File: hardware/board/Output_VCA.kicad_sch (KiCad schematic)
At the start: 23 parts

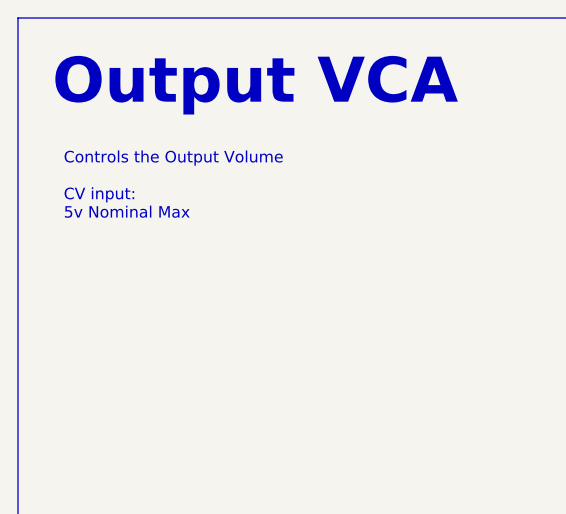
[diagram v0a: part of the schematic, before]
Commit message: Schematic getting closer to being finished
Schematic should be close to being ready to assign MPNs.
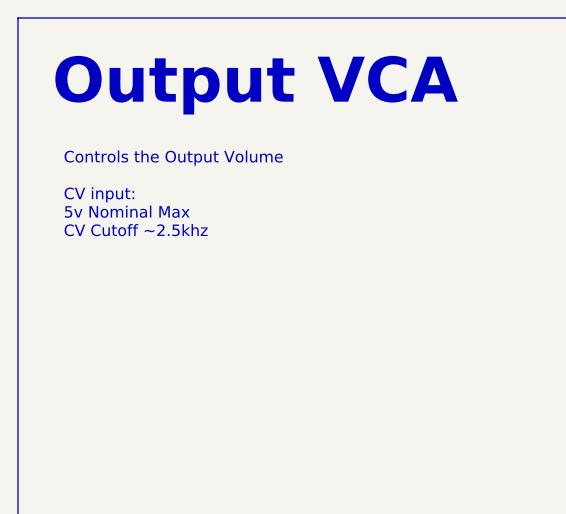
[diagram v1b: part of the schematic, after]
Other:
- note added: "Controls the Output Volume CV input: 5v Nominal Max CV Cutoff ~2.5khz"
- note removed: "Controls the Output Volume CV input: 5v Nominal Max"
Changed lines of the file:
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@@
     (fill (type none))
   )
-  (text "Controls the Output Volume\n\nCV input:\n5v Nominal Max\n\n\n"
+  (text "Controls the Output Volume\n\nCV input:\n5v Nominal Max\nCV Cutoff ~2.5khz\n\n"
     (at 27.94 49.53 0)
     (effects (font (size 1.27 1.27)) (justify left bottom))

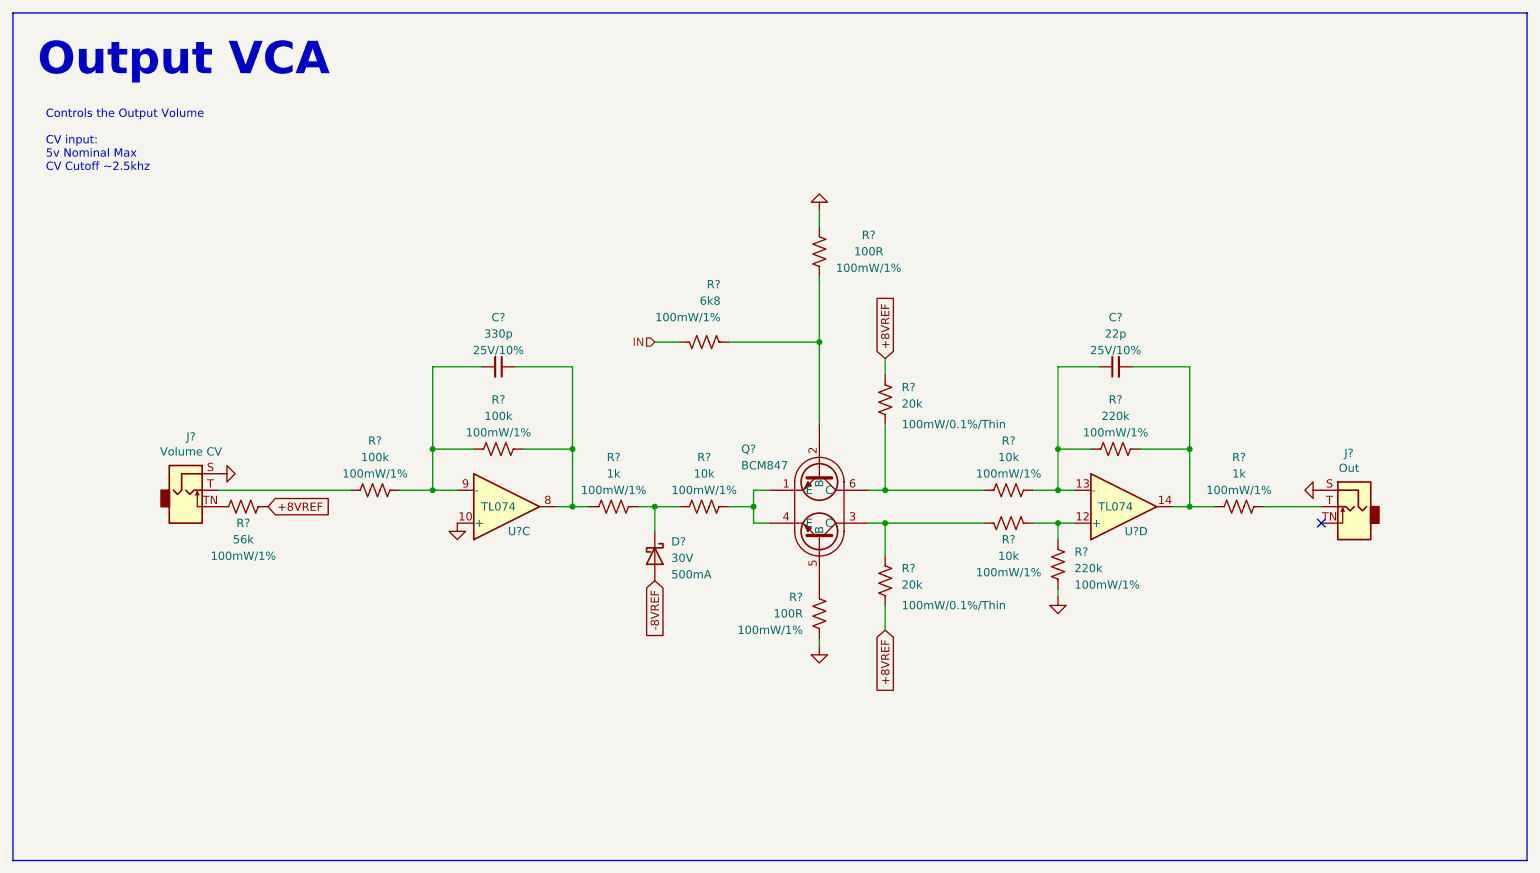
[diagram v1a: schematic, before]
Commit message: BOM Consolidation
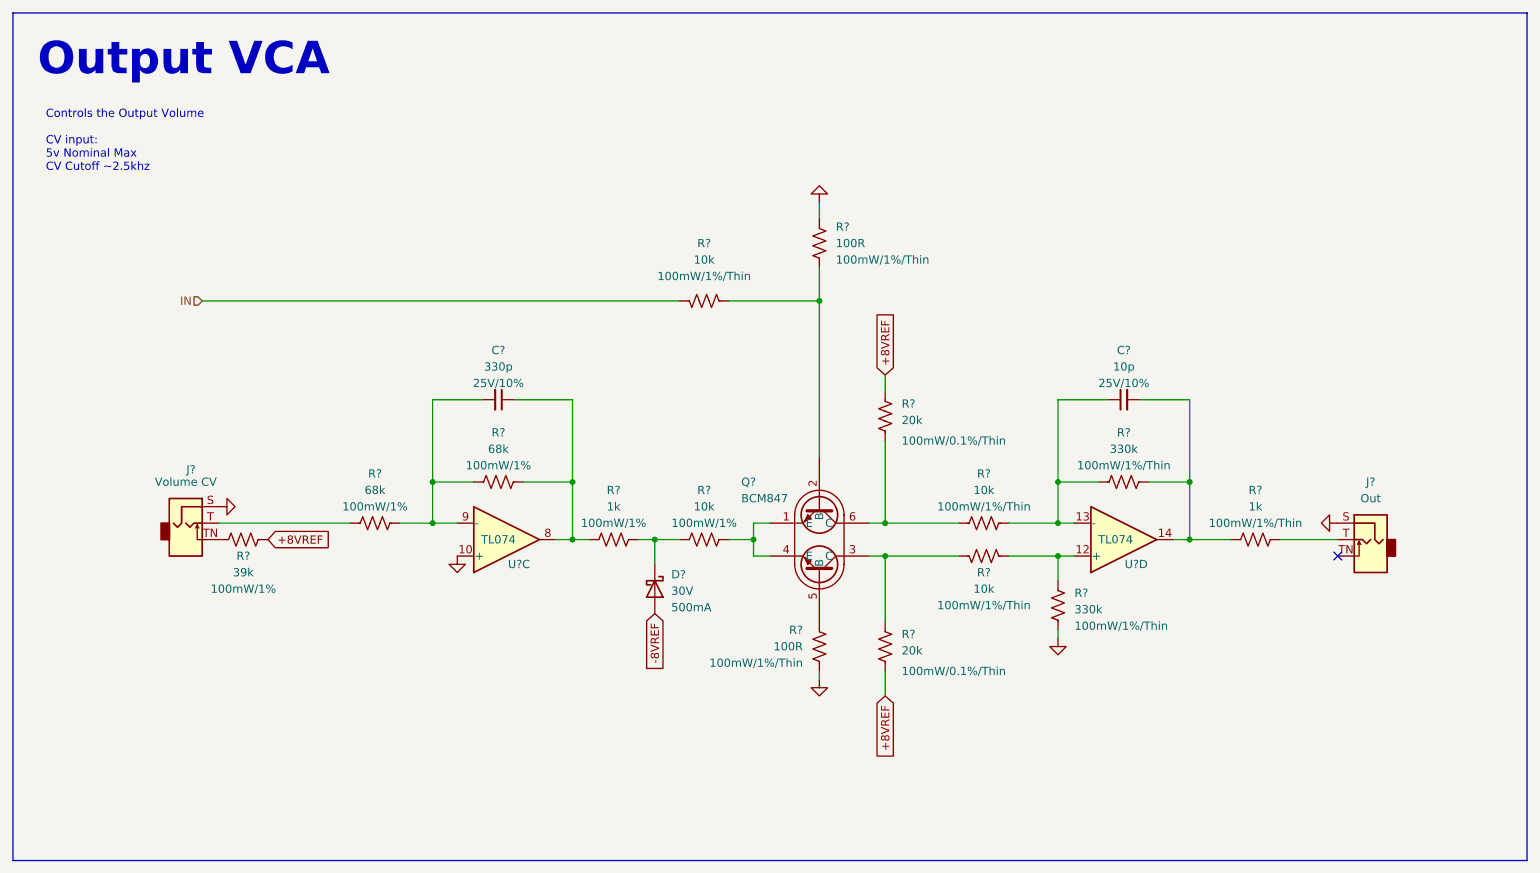
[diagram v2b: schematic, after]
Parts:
- C?: value 22p -> 10p
- J?: value Out -> ~; Name (none) -> Out
- J?: value Volume CV -> ~; Name (none) -> Volume CV
- R? (x2): value 100k -> 68k
- R?: value 6k8 -> 10k; Rating 100mW/1% -> 100mW/1%/Thin
- R? (x5): Rating 100mW/1% -> 100mW/1%/Thin
- R? (x2): value 220k -> 330k; Rating 100mW/1% -> 100mW/1%/Thin
- R?: value 56k -> 39k
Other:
- moved on the sheet: C?, D?, J?, Q?, R?, U?C, U?D

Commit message: Updates for LED Drivers
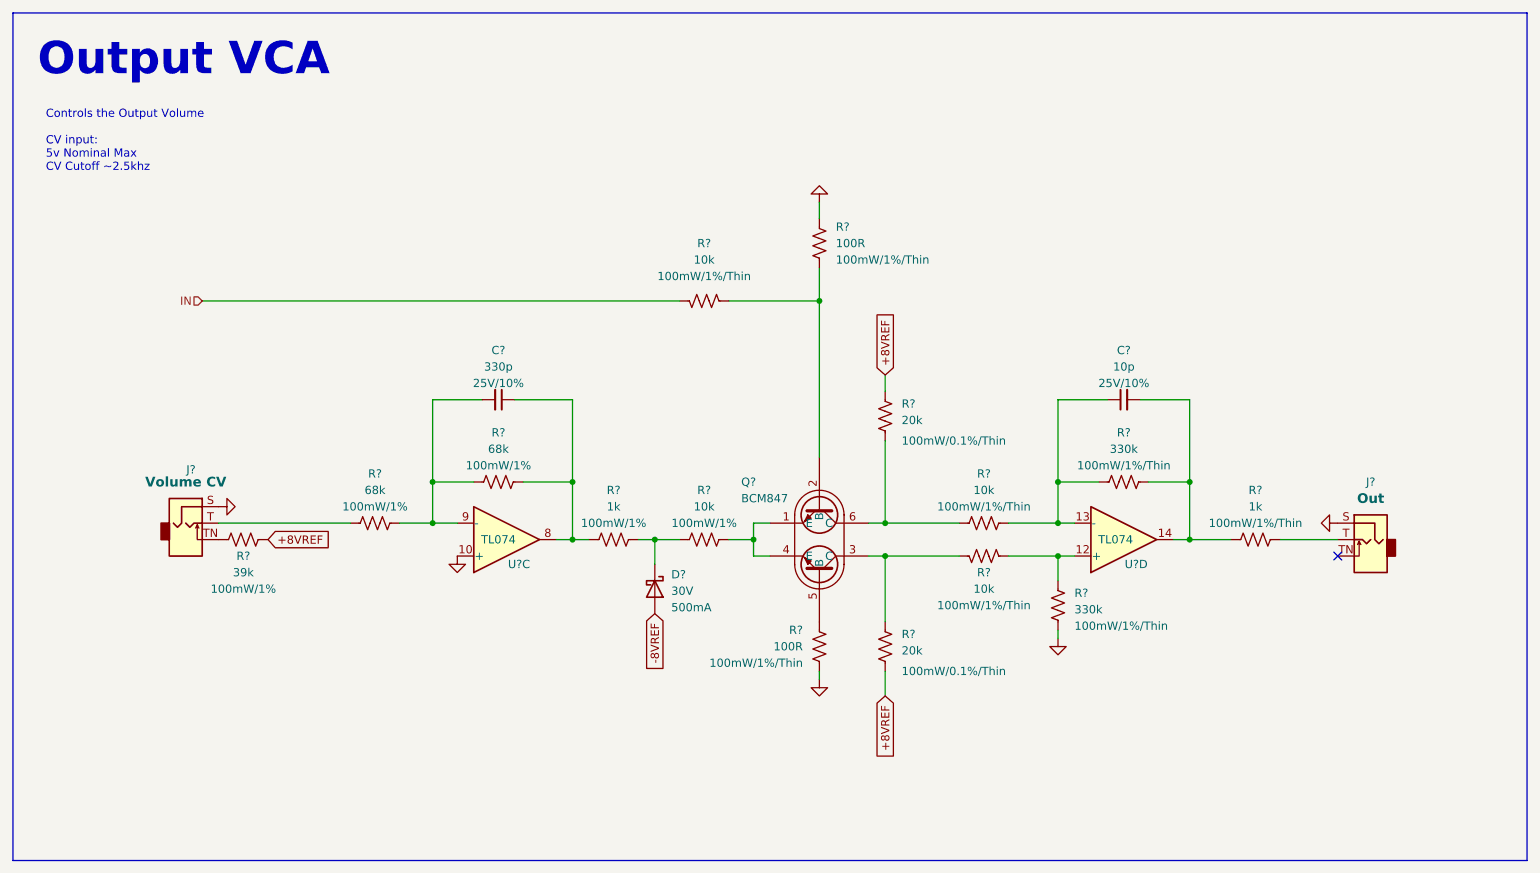
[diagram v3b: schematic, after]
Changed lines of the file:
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@@
     )
     (property "Name" "Out" (at 232.41 97.79 0)
-      (effects (font (size 1.27 1.27)))
+      (effects (font (size 1.5 1.5) bold))
     )
     (pin "S")
@@
     )
     (property "Name" "Volume CV" (at 49.53 95.25 0)
-      (effects (font (size 1.27 1.27)))
+      (effects (font (size 1.5 1.5) bold))
     )
     (pin "S")

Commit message: hardware: update schematic with footprints and preliminary MPNs
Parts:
- C? (x2): Notes 0603, 25V+, 10% -> (none); smd kit 1 -> (none)
- D?: value 30V -> BAS315; footprint winterbloom:D_SOD-123+SOD-123F -> winterbloom:D_SOD-323; MPN (none) -> BAS316,115; Notes Any PMEGxxxxEGW part, 500mA If -> Clipping diode; Rating 500mA -> 1Vf @ 100mA; mpn PMEG2005EGWX -> (none); smd kit 1 -> (none)
- J? (x2): mpn WQP-WQP518MA -> (none)
- Q?: LCSC C396099 -> (none); LCSC Extended YES -> (none); Manufacturer Nexperia -> (none)
- R? (x15): smd kit 1 -> (none)
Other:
- title: Diode Ladder Filter -> Neptune

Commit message: Very first component layout.
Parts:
- removed U?: TL074, Package_SO:TSSOP-14_4.4x5mm_P0.65mm, symbol winterbloom:TL074
- added U?: TL074, Package_SO:TSSOP-14_4.4x5mm_P0.65mm, symbol winterbloom:TL074
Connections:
- net GND: now also U?.12 (+)
- net at C?.2, R?.1, R?.2: now also U?.13 (-)
- net at R?.1, R?.1: now also U?.3 (+); no longer U?.12 (+)
- net at C?.2, R?.1, R?.2: now also U?.1; no longer U?.14
- net at C?.1, R?.1, R?.2: now also U?.2 (-); no longer U?.13 (-)
- net at C?.1, R?.1, R?.2: now also U?.14
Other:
- moved on the sheet: U?D

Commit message: First Draft of layout V2 (All components facing the same way)
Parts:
- removed U? (x2): TL074, Package_SO:TSSOP-14_4.4x5mm_P0.65mm, symbol winterbloom:TL074
- added U? (x2): TL074, Package_SO:TSSOP-14_4.4x5mm_P0.65mm, symbol winterbloom:TL074
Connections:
- net GND: now also U?.10 (+)
- net at C?.2, R?.1, R?.2: now also U?.9 (-)
- net at R?.1, R?.1: now also U?.5 (+)
- net at C?.2, R?.1, R?.2: now also U?.7
- net at C?.1, R?.1, R?.2: now also U?.6 (-)
- net at C?.1, R?.1, R?.2: now also U?.8

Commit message: Rough Draft of Routing Complete. Ugly but Passes DRC
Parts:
- removed D?: BAS315, winterbloom:D_SOD-323, symbol Diode:1N5819
- added D?: BAS315, winterbloom:D_SOD-323, symbol Device:D_Small
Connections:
- net -8VREF: now also D?.2 (A)
- net at R?.1, R?.2: now also D?.1 (K)
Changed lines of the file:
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@@
+    (stroke (width 0) (type default))
+  )
+  (wire (pts (xy 121.92 113.03) (xy 121.92 115.57))
     (stroke (width 0) (type default))
   )
@@
     )
   )
+  (symbol (lib_id "Device:D_Small") (at 121.92 110.49 90) (mirror x) (unit 1)
+    (in_bom yes) (on_board yes) (dnp no)
+    (property "Reference" "D?" (at 131.445 107.95 90)
+      (effects (font (size 1.27 1.27)))
+    )
+    (property "Value" "BAS315" (at 131.445 110.49 90)
+      (effects (font (size 1.27 1.27)))
+    )
+    (property "Footprint" "winterbloom:D_SOD-323" (at 121.92 110.49 90)
+      (effects (font (size 1.27 1.27)) hide)
+    )
+    (property "Datasheet" "~" (at 121.92 110.49 90)
+      (effects (font (size 1.27 1.27)) hide)
+    )
+    (property "MPN" "BAS316,115" (at 121.92 110.49 0)
+      (effects (font (size 1.27 1.27)) hide)
+    )
+    (property "Rating" "1Vf @ 100mA" (at 131.445 113.03 90)
+      (effects (font (size 1.27 1.27)))
+    )
+    (property "Notes" "Clipping diode" (at 121.92 110.49 0)
+      (effects (font (size 1.27 1.27)) hide)
+    )
+    (pin "1")
+    (pin "2")
+    (instances
+      (project "mainboard"
+        (path "/960bd036-bf0c-45ea-9f41-1321756e0e5a"
+          (reference "D?") (unit 1)
+        )
+        (path "/960bd036-bf0c-45ea-9f41-1321756e0e5a/3b1fa3f2-493c-449c-a2d6-10ea677680a0"
+          (reference "D?") (unit 1)
+        )
+        (path "/960bd036-bf0c-45ea-9f41-1321756e0e5a/48d891c0-35ba-4c8e-a930-c990a10298eb"
+          (reference "D601") (unit 1)
+        )
+        (path "/960bd036-bf0c-45ea-9f41-1321756e0e5a/0f8a3c3e-e197-47b5-881d-2ae4e2374020"
+          (reference "D701") (unit 1)
+        )
+        (path "/960bd036-bf0c-45ea-9f41-1321756e0e5a/2f882567-d4bc-4d02-ab1f-fc30e1722a04"
+          (reference "D801") (unit 1)
+        )
+      )
+      (project "Diode_Ladder_Filter_V0.5"
+        (path "/e63e39d7-6ac0-4ffd-8aa3-1841a4541b55"
+          (reference "D?") (unit 1)
+        )
+      )
+    )
+  )
   (symbol (lib_name "BCM847_1") (lib_id "Carson's Schematic Symbols:BCM847") (at 147.32 104.14 270) (unit 1)
     (in_bom yes) (on_board yes) (dnp no)
@@
         )
       )
-    )
-  )
-  (symbol (lib_id "Diode:1N5819") (at 121.92 111.76 270) (unit 1)
-    (in_bom yes) (on_board yes) (dnp no) (fields_autoplaced)
-    (property "Reference" "D?" (at 124.46 109.5375 90)
-      (effects (font (size 1.27 1.27)) (justify left))
-    )
-    (property "Value" "BAS315" (at 124.46 112.0775 90)
-      (effects (font (size 1.27 1.27)) (justify left))
-    )
-    (property "Footprint" "winterbloom:D_SOD-323" (at 117.475 111.76 0)
-      (effects (font (size 1.27 1.27)) hide)
-    )
-    (property "Datasheet" "http://www.vishay.com/docs/88525/1n5817.pdf" (at 121.92 111.76 0)
-      (effects (font (size 1.27 1.27)) hide)
-    )
-    (property "Notes" "Clipping diode" (at 121.92 111.76 0)
-      (effects (font (size 1.27 1.27)) hide)
-    )
-    (property "Rating" "1Vf @ 100mA" (at 124.46 114.6175 90)
-      (effects (font (size 1.27 1.27)) (justify left))
-    )
-    (property "MPN" "BAS316,115" (at 121.92 111.76 0)
-      (effects (font (size 1.27 1.27)) hide)
-    )
-    (pin "1")
-    (pin "2")
-    (instances
-      (project "board"
-        (path "/55082cc1-c956-45a6-b2b5-3db02a6da9d0"
-          (reference "D?") (unit 1)
-        )
-      )
-      (project "mainboard"
-        (path "/960bd036-bf0c-45ea-9f41-1321756e0e5a/48d891c0-35ba-4c8e-a930-c990a10298eb"
-          (reference "D?") (unit 1)
-        )
-        (path "/960bd036-bf0c-45ea-9f41-1321756e0e5a/0f8a3c3e-e197-47b5-881d-2ae4e2374020"
-          (reference "D?") (unit 1)
-        )
-        (path "/960bd036-bf0c-45ea-9f41-1321756e0e5a/2f882567-d4bc-4d02-ab1f-fc30e1722a04"
-          (reference "D801") (unit 1)
-        )
-      )
-      (project "VCA"
-        (path "/de69ad6f-07bb-4f9c-962b-520f6532317d"
-          (reference "D?") (unit 1)
-        )
-        (path "/de69ad6f-07bb-4f9c-962b-520f6532317d/0f818280-e6cd-4382-a215-72bb59f50cc3"
-          (reference "D?") (unit 1)
-        )
-      )

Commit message: hardware: minor fixes and aesthetic updates
- Fix HP LEDs being backwards
- Switch power header, pot, and jack footprints to longpad variants
- Make the text size on the front side larger
- Add "red" and "blue" text next to respective LEDs on front side
- Adjusted zone thermal spoke for better connection to GND pads
- Squished the solder jumpers for instability type closer together
- Minor adjustments to traces to accommodate longpad footprints
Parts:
- J? (x2): footprint winterbloom:AudioJack_WQP518MA_Compact_S -> winterbloom:AudioJack_WQP518MA_Compact_S_LongPads
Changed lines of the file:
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@@
       (effects (font (size 1.27 1.27)))
     )
-    (property "Footprint" "winterbloom:AudioJack_WQP518MA_Compact_S" (at 233.68 96.52 0)
+    (property "Footprint" "winterbloom:AudioJack_WQP518MA_Compact_S_LongPads" (at 233.68 96.52 0)
       (effects (font (size 1.27 1.27)) hide)
     )
@@
       (effects (font (size 1.27 1.27)))
     )
-    (property "Footprint" "winterbloom:AudioJack_WQP518MA_Compact_S" (at 48.26 93.98 0)
-      (effects (font (size 1.27 1.27)) hide)
-    )
+    (property "Footprint" "winterbloom:AudioJack_WQP518MA_Compact_S_LongPads" (at 48.26 93.98 0)
+      (effects (font (size 1.27 1.27)) hide)
+    )
